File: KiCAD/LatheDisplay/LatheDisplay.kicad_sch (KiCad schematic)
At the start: 9 parts, among them U1 D168K, U2 D168K, U3 D168K, U4 D168K, U5 D168K, U6 ICM7218B, U7 ATmega328-P, U9 INA821xD

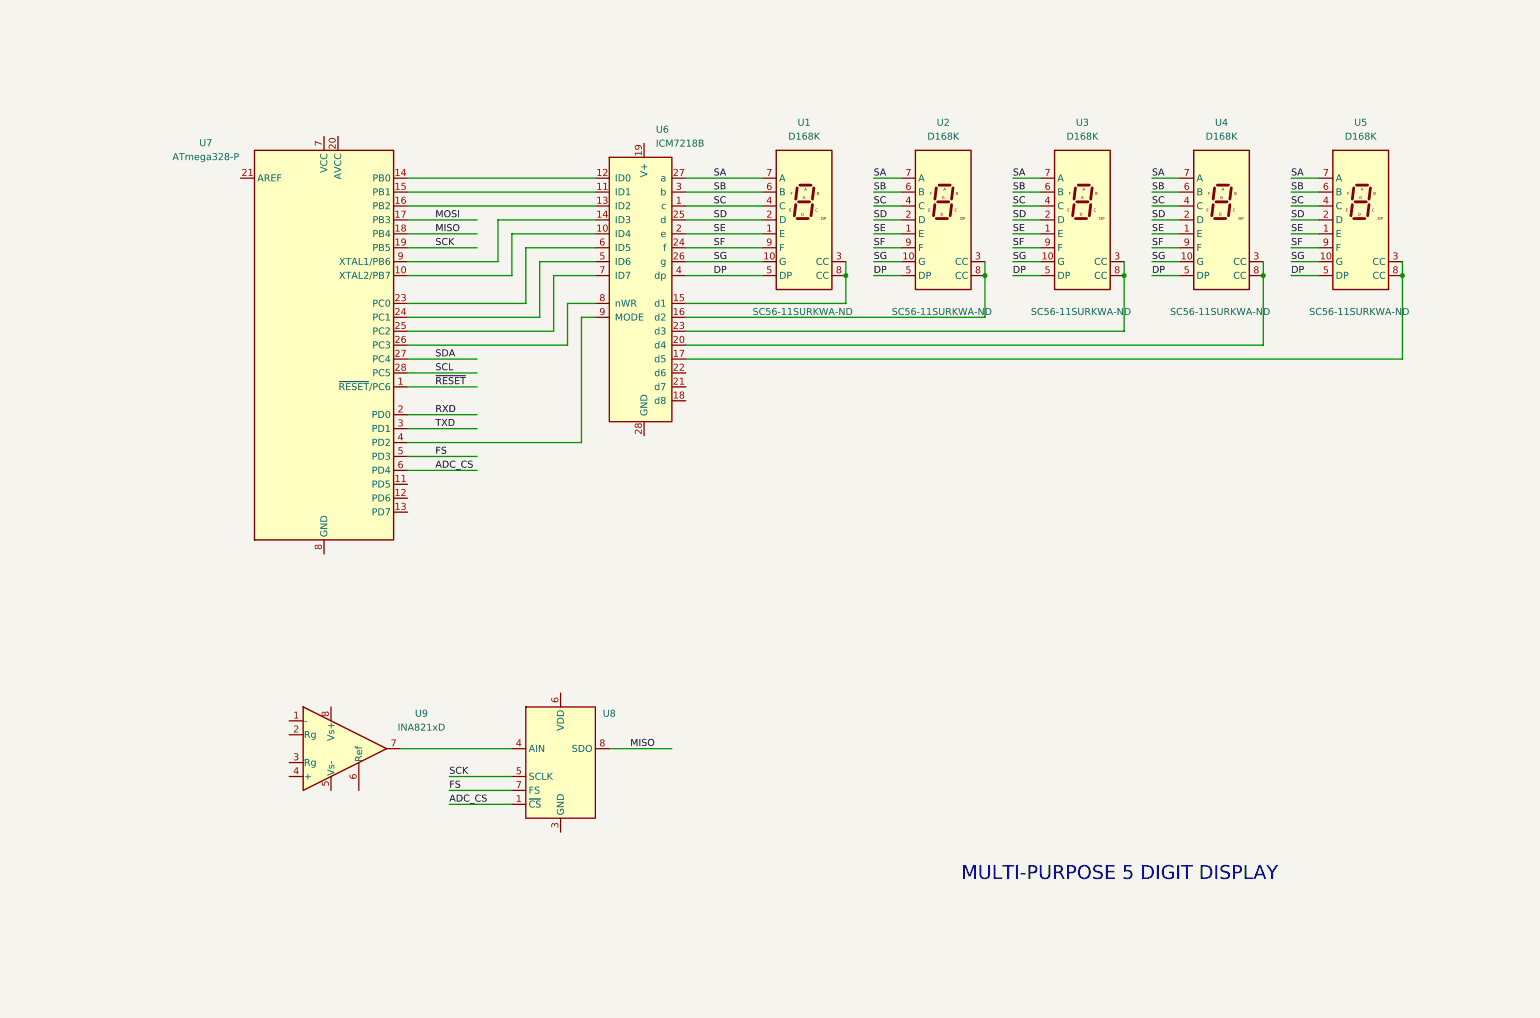
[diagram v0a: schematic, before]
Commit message: components assigned and tentative placement
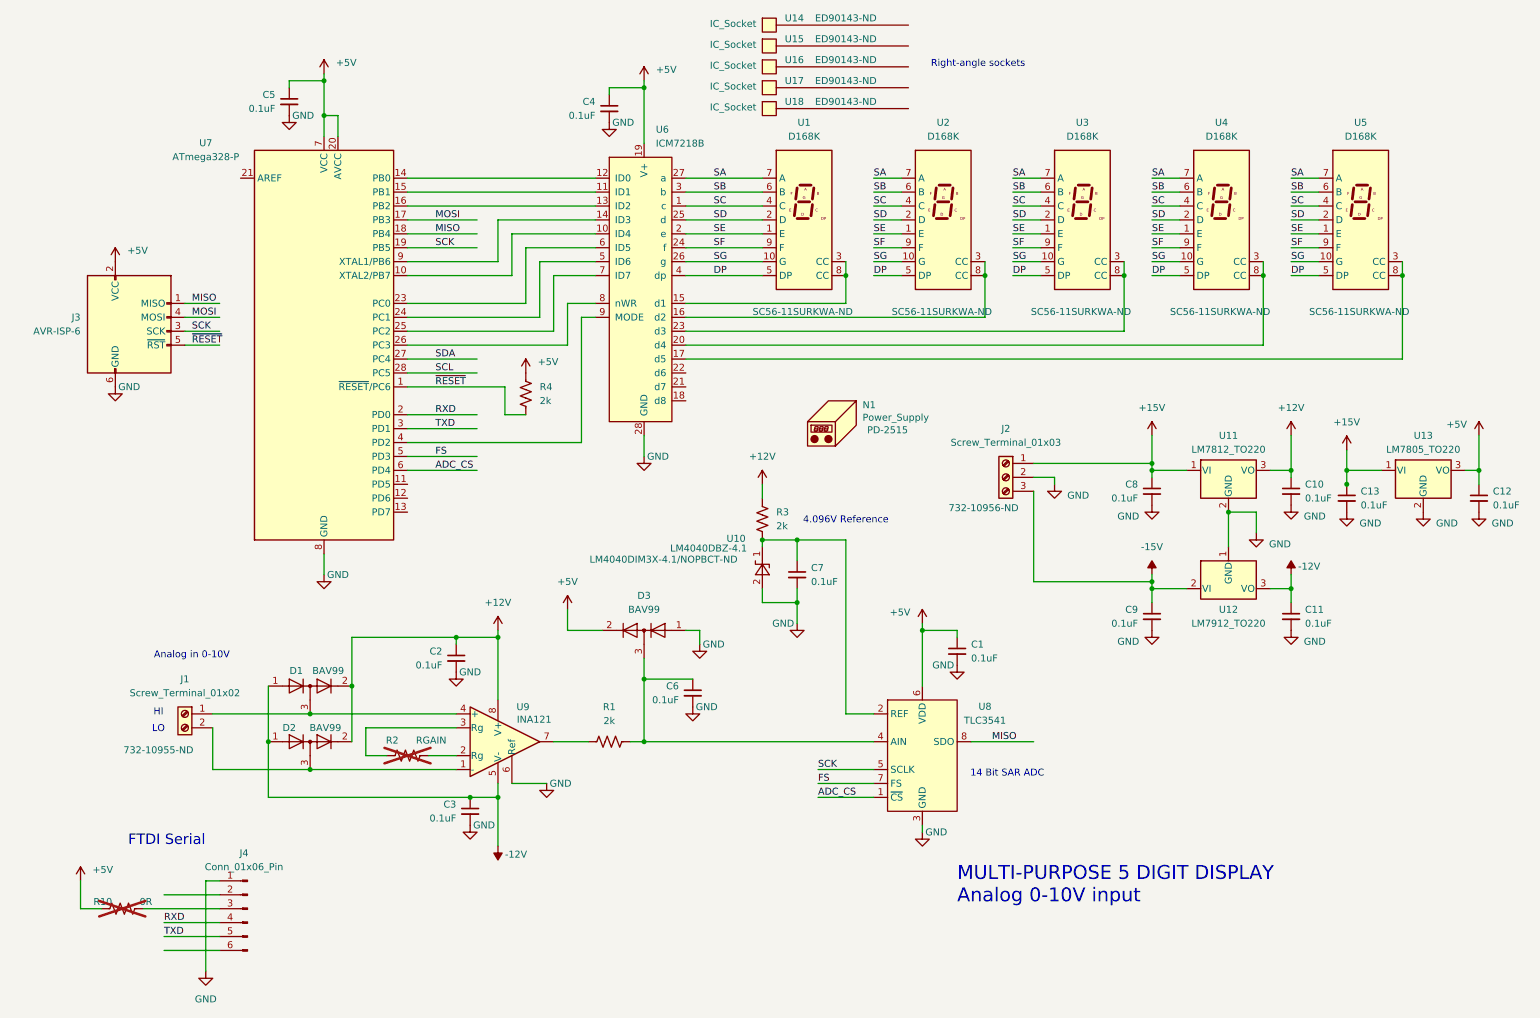
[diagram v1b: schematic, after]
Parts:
- removed U9: INA821xD, Package_SO:SOIC-8_3.9x4.9mm_P1.27mm, symbol Amplifier_Instrumentation:INA821xD
- added C1, C10, C11, C12, C13, C2, C3, C4, C5, C6, C7, C8, C9: 0.1uF, Capacitor_SMD:C_1206_3216Metric_Pad1.33x1.80mm_HandSolder, symbol Device:C_Small
- added D1, D2, D3: BAV99, Package_TO_SOT_SMD:SOT-23, symbol Diode:BAV99
- added J1: Screw_Terminal_01x02, models:691137710002, symbol Connector:Screw_Terminal_01x02
- added J2: Screw_Terminal_01x03, models:3-pin-terminal, symbol Connector:Screw_Terminal_01x03
- added J3: AVR-ISP-6, Connector_PinHeader_2.54mm:PinHeader_2x03_P2.54mm_Vertical, symbol Connector:AVR-ISP-6
- added J4: Conn_01x06_Pin, Connector_PinHeader_2.54mm:PinHeader_1x06_P2.54mm_Horizontal, symbol Connector:Conn_01x06_Pin
- added N1: Power_Supply, symbol Mechanical:Housing
- added R1, R3, R4: 2k, Resistor_SMD:R_1206_3216Metric_Pad1.30x1.75mm_HandSolder, symbol Device:R_US
- added R10: 0R, Resistor_SMD:R_1206_3216Metric_Pad1.30x1.75mm_HandSolder, symbol Device:R_US
- added R2: RGAIN, Resistor_SMD:R_1206_3216Metric_Pad1.30x1.75mm_HandSolder, symbol Device:R_US
- added U10: LM4040DBZ-4.1, Package_TO_SOT_SMD:SOT-23, symbol Reference_Voltage:LM4040DBZ-4.1
- added U11: LM7812_TO220, Package_TO_SOT_THT:TO-220-3_Vertical, symbol Regulator_Linear:LM7812_TO220
- added U12: LM7912_TO220, Package_TO_SOT_THT:TO-220-3_Vertical, symbol Regulator_Linear:LM7912_TO220
- added U13: LM7805_TO220, Package_TO_SOT_THT:TO-220-3_Vertical, symbol Regulator_Linear:LM7805_TO220
- added U14, U15, U16, U17, U18: IC_Socket, symbol misc_bom:BOM_item
- added U9: INA121, Package_SO:SO-8_3.9x4.9mm_P1.27mm, symbol INA121:INA121
- U1, U2, U3, U4, U5: footprint Display_7Segment:D1X8K -> Package_DIP:DIP-10_W7.62mm_LongPads
- U6: footprint (none) -> Package_DIP:DIP-28_W7.62mm_LongPads
- U7: CatNo (none) -> ATMEGA328-PU-ND
- U8: value ~ -> TLC3541; footprint (none) -> Package_SO:SO-8_3.9x4.9mm_P1.27mm; CatNo (none) -> 296-12498-5-ND
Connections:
- net MISO: now also J3.1 (MISO)
- net MOSI: now also J3.4 (MOSI)
- net RXD: now also J4.4 (Pin_4)
- net SCK: now also J3.3 (SCK)
- net TXD: now also J4.5 (Pin_5)
- net ~{RESET}: now also J3.5 (~{RST}), R4.1
- net GND: now reaches U8.3 (GND)
- net GND: now also U6.28 (GND), U7.22 (GND), U7.8 (GND), C1.2, C10.2, C11.2, C12.2, C13.2, C2.2, C3.2, C4.2, C5.2, C6.2, C7.2, C8.2, C9.2, D3.1 (K), J2.2 (Pin_2), J3.6 (GND), J4.1 (Pin_1), U10.2 (A), U11.2 (GND), U12.1 (GND), U13.2 (GND), U9.6 (Ref)
- net at U8.4 (AIN): now also C6.1, D3.3 (K), R1.2
- net +5V: now reaches U8.6 (VDD)
- net +5V: now also U6.19 (V+), U7.20 (AVCC), U7.7 (VCC), C1.1, C12.1, C4.1, C5.1, D3.2 (A), J3.2 (VCC), R10.1, R4.2, U13.3 (VO)
- new net: J4.3 (Pin_3), R10.2
- new net: C7.1, R3.1, U10.1 (K), U8.2 (REF)
- new net: R2.1, U9.3 (Rg)
- new net: R2.2, U9.2 (Rg)
- new net: D1.3 (K), J1.1 (Pin_1), U9.4 (+)
- new net: D2.3 (K), J1.2 (Pin_2), U9.1 (-)
- new net: R1.1, U9.7
- new net +12V: C10.1, C2.1, D1.2 (A), D2.2 (A), R3.2, U11.3 (VO), U9.8 (V+)
- new net +15V: C13.1, C8.1, J2.1 (Pin_1), U11.1 (VI), U13.1 (VI)
- new net -12V: C11.1, C3.1, D1.1 (K), D2.1 (K), U12.3 (VO), U9.5 (V-)
- new net -15V: C9.1, J2.3 (Pin_3), U12.2 (VI)
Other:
- note added: "14 Bit SAR ADC"
- note added: "4.096V Reference"
- note added: "Analog in 0-10V"
- note added: "FTDI Serial"
- note added: "HI"
- note added: "LO"
- note added: "MULTI-PURPOSE 5 DIGIT DISPLAY Analog 0-10V input"
- note added: "Right-angle sockets"
- note removed: "MULTI-PURPOSE 5 DIGIT DISPLAY"

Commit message: save lathe stuff
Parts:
- removed J2: Screw_Terminal_01x03, models:3-pin-terminal, symbol Connector:Screw_Terminal_01x03
- removed N1: Power_Supply, symbol Mechanical:Housing
- added J5: Screw_Terminal_01x02, models:691137710002, symbol Connector:Screw_Terminal_01x02
- added VR1: IE2424S, symbol my_DCDC:IE2424S
- J4: footprint Connector_PinHeader_2.54mm:PinHeader_1x06_P2.54mm_Horizontal -> Connector_PinHeader_2.54mm:PinHeader_1x06_P2.54mm_Vertical
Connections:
- net GND: now also J5.2 (Pin_2), VR1.1 (VIN-), VR1.4 (VOUT+)
- net +15V: no longer names the net of C13.1, U13.1 (VI)
- net +15V: no longer C8.1, U11.1 (VI)
- net -15V renamed -24V
- net -24V: now also VR1.3 (VOUT-)
- new net +24V: C8.1, J5.1 (Pin_1), U11.1 (VI), VR1.2 (VIN+)
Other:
- moved on the sheet: C10, C11, C12, C13, C8, C9, U11, U12, U13
